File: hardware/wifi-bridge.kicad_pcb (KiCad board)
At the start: 2 copper layers, 63 parts, among them J101 USB-MINI-B-SMD, P201 CON-SENSOR, Q201 MOS_P, SW201 ERASE, SW202 RESET, U101 AT91SAM3SXB, U102 82400152, U103 AAT3681A, U104 PAM2301, U105 FAN4860, U201 ESP8266_WROOM02, U202 M24C64, X201 16MHz

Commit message: new placement idea
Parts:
- removed BT101: BATTERY, kicad-libraries:JST-PH-SM4-2
- removed C110, C111, C112, C115, C116: 100nF, kicad-libraries:0603E
- removed C113, C117: 10µF, kicad-libraries:0805E
- removed C114, C120, C121: 4.7µF, kicad-libraries:0603E
- removed C118, C119: 2.2µF, kicad-libraries:0603E
- removed D201: LED, kicad-libraries:D0603
- removed F101: PTC, kicad-libraries:1206E
- removed FILTER201: Filter-8x, kicad-libraries:DFN16-33x135
- removed J101: USB-MINI-B-SMD, kicad-libraries:USB-MINI-B-SMD
- removed L103: FB, kicad-libraries:0603E
- removed L104: LBR2012T100K, kicad-libraries:0805E
- removed L105: 1µH, kicad-libraries:0805E
- removed L106: 4.7µH, kicad-libraries:0805E
- removed P201: CON-SENSOR, kicad-libraries:CON-SENSOR
- removed Q201: MOS_P, kicad-libraries:SOT23GDS
- removed R104: 3.24k, kicad-libraries:0603E
- removed R105: 470k, kicad-libraries:0603E
- removed R106: 1M, kicad-libraries:0603E
- removed RP201: 4k7, kicad-libraries:0603X4
- removed SW201: ERASE, kicad-libraries:SW_06_SMD
- removed SW202: RESET, kicad-libraries:SW_06_SMD
- removed X201: 16MHz, kicad-libraries:CRYSTAL_3225
- added BT201: BATTERY, kicad-libraries:JST-PH-SM4-2, F.Cu at (24.6, 11.8)
- added C210: 100nF, kicad-libraries:0603E, F.Cu at (-7.47, 11.4)
- added C211: 100nF, kicad-libraries:0603E, F.Cu at (11.6, -2.10)
- added C212: 100nF, kicad-libraries:0603E, F.Cu at (8.95, -0.25)
- added C213: 10µF, kicad-libraries:0805E, F.Cu at (-16.5, -12.2)
- added C214: 4.7µF, kicad-libraries:0603E, F.Cu at (-21.9, -5.95)
- added C215: 100nF, kicad-libraries:0603E, F.Cu at (-23.2, -8.47)
- added C216: 100nF, kicad-libraries:0603E, F.Cu at (-24.8, -1.32)
- added C217: 10µF, kicad-libraries:0805E, F.Cu at (-30.4, -5.58)
- added C218: 2.2µF, kicad-libraries:0603E, F.Cu at (-29.1, -1.15)
- added C219: 2.2µF, kicad-libraries:0603E, F.Cu at (-31.4, -11.2)
- added C220: 4.7µF, kicad-libraries:0603E, F.Cu at (-10.0, -7.12)
- added C221: 4.7µF, kicad-libraries:0603E, F.Cu at (-5.83, -12.1)
- added D101: LED, kicad-libraries:D0603, F.Cu at (-7.47, -9.53)
- added F201: PTC, kicad-libraries:1206E, F.Cu at (163.2, 19.4)
- added FILTER101: Filter-8x, kicad-libraries:DFN16-33x135, F.Cu at (157.5, 47.4)
- added J201: USB-MINI-B-SMD, kicad-libraries:USB-MINI-B-SMD, F.Cu at (155.8, 15.2)
- added L201: FB, kicad-libraries:0603E, F.Cu at (-3.60, -3.70)
- added L202: 744230900, kicad-libraries:WE-CNSW-0603, F.Cu at (153.3, 26.6)
- added L203: FB, kicad-libraries:0603E, F.Cu at (-2.45, -11.4)
- added L204: LBR2012T100K, kicad-libraries:0805E, F.Cu at (-22.4, -13.8)
- added L205: 1µH, kicad-libraries:0805E, F.Cu at (-15.9, -0.23)
- added L206: 4.7µH, kicad-libraries:0805E, F.Cu at (-1.30, -13.3)
- added P101: CON-SENSOR, kicad-libraries:CON-SENSOR, F.Cu at (155.8, 55.2)
- added Q101: MOS_P, kicad-libraries:SOT23GDS, F.Cu at (-25.4, 4.10)
- added R204: 3.24k, kicad-libraries:0603E, F.Cu at (1.93, -8.88)
- added R205: 470k, kicad-libraries:0603E, F.Cu at (2.00, -6.75)
- added R206: 1M, kicad-libraries:0603E, F.Cu at (-1.57, -5.03)
- added RP101: 4k7, kicad-libraries:0603X4, F.Cu at (-9.38, -2.25)
- added SW101: ERASE, kicad-libraries:SW_06_SMD, F.Cu at (4.05, -20.6)
- added SW102: RESET, kicad-libraries:SW_06_SMD, F.Cu at (-13.4, -21.5)
- added U106: DRILL, kicad-libraries:DRILL_NP, F.Cu at (125.3, 17.7)
- added U107: DRILL, kicad-libraries:DRILL_NP, F.Cu at (170.3, 17.7)
- added U203: PAM2301, kicad-libraries:TSOT-25, F.Cu at (-15.1, -4.40)
- added U204: FAN4860, kicad-libraries:UMLP_22, F.Cu at (-17.2, 5.45)
- added X101: 16MHz, kicad-libraries:CRYSTAL_3225, F.Cu at (-2.45, -7.72)
- C101: value 10µF -> 100nF; footprint kicad-libraries:0805E -> kicad-libraries:0603E
- C102: value 100nF -> 470µF; footprint kicad-libraries:0603E -> kicad-libraries:ELKO_63
- C103: value 4.7µF -> 100nF
- C104, C105: value 100nF -> DNP
- C106, C108: value 100nF -> 1µF
- C107: value 2.2µF -> 1µF
- C201: value 100nF -> 10µF; footprint kicad-libraries:0603E -> kicad-libraries:0805E
- C202: value 470µF -> 100nF; footprint kicad-libraries:ELKO_83 -> kicad-libraries:0603E
- C203: value 100nF -> 4.7µF
- C204, C205: value DNP -> 100nF
- C206, C208: value 1µF -> 100nF
- C207: value 1µF -> 2.2µF
- L101: value FB -> INDUCT
- L102: value 744230900 -> INDUCT
- R101, R102: value 27 -> 10k
- R103: value 1R0 -> 2k2
- R201, R202: value 10k -> 27
- R203: value 2k2 -> 1R0
- U102: value 82400152 -> ESP8266_WROOM02; footprint kicad-libraries:SOT563-SPEC -> kicad-libraries:ESP8266_WROOM02
- U103: value AAT3681A -> M24C64; footprint kicad-libraries:SC70JW-8 -> kicad-libraries:SOIC8
- U104: value PAM2301 -> DRILL; footprint kicad-libraries:TSOT-25 -> kicad-libraries:DRILL_NP
- U105: value FAN4860 -> DRILL; footprint kicad-libraries:UMLP_22 -> kicad-libraries:DRILL_NP
- U201: value ESP8266_WROOM02 -> 82400152; footprint kicad-libraries:ESP8266_WROOM02 -> kicad-libraries:SOT563-SPEC
- U202: value M24C64 -> AAT3681A; footprint kicad-libraries:SOIC8 -> kicad-libraries:SC70JW-8
- moved U201 104.6 mm to (156.2, 25.7), turned to 180 degrees
- moved R201 90.6 mm to (150.2, 25.9), turned to 180 degrees
- moved R202 89.8 mm to (150.2, 27.3), turned to 180 degrees
- moved U101 88.4 mm to (155.8, 36.2)
- moved C102 79.4 mm to (127.7, 45.5), turned to 180 degrees
- moved C101 71.6 mm to (131.0, 41.4)
- moved U102 69.4 mm to (133.0, 30.1)
- moved U104 56.7 mm to (170.3, 52.7)
- moved U105 51.1 mm to (125.3, 52.7)
- moved U202 51.0 mm to (118.6, 116.5)
- moved R102 45.1 mm to (140.7, 88.8)
- moved L102 44.9 mm to (141.1, 76.6)
- moved R101 20.1 mm to (115.7, 93.5)
- moved L101 15.9 mm to (139.9, 105.6)
- moved C202 4.72 mm to (181.1, 120.7)
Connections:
- C103 pad 1: 3V3 -> GND
- C103 pad 2: GND -> 3V3
- C104 pad 1: 3V3 -> Net-(C104-Pad1)
- C105 pad 1: 3V3 -> Net-(C105-Pad1)
- C108 pad 1: Net-(C107-Pad1) -> +5V
- C203 pad 1: GND -> 3V3
- C203 pad 2: 3V3 -> GND
- C204 pad 1: Net-(C204-Pad1) -> 3V3
- C205 pad 1: Net-(C205-Pad1) -> 3V3
- C208 pad 1: +5V -> Net-(C207-Pad1)
- L101 pad 1: GND -> Net-(C107-Pad1)
- L101 pad 2: Net-(J101-Pad6) -> 3V3
- L102 pad 1: Net-(L102-Pad1) -> Net-(C109-Pad1)
- L102 pad 2: Net-(L102-Pad2) -> +5V
- L102 pad 3: Net-(L102-Pad3) -> (no net)
- L102 pad 4: Net-(L102-Pad4) -> (no net)
- R101 pad 1: Net-(L102-Pad1) -> (no net)
- R101 pad 2: (no net) -> Net-(R101-Pad2)
- R102 pad 1: Net-(L102-Pad4) -> (no net)
- R102 pad 2: (no net) -> Net-(R102-Pad2)
- R103 pad 1: Net-(C115-Pad1) -> 3V3
- R201 pad 1: (no net) -> Net-(L202-Pad1)
- R201 pad 2: Net-(R201-Pad2) -> D+
- R202 pad 1: (no net) -> Net-(L202-Pad4)
- R202 pad 2: Net-(R202-Pad2) -> D-
- R203 pad 1: 3V3 -> Net-(C215-Pad1)
- U101 pad 1: (no net) -> 3V3
- U101 pad 12: (no net) -> Net-(C207-Pad1)
- U101 pad 17: (no net) -> GND
- U101 pad 18: (no net) -> 3V3
- U101 pad 2: (no net) -> GND
- U101 pad 24: (no net) -> Net-(C207-Pad1)
- U101 pad 39: (no net) -> Net-(SW102-Pad1)
- U101 pad 45: (no net) -> 3V3
- U101 pad 46: (no net) -> GND
- U101 pad 54: (no net) -> Net-(C207-Pad1)
- U101 pad 55: (no net) -> Net-(SW101-Pad1)
- U101 pad 56: (no net) -> D-
- U101 pad 57: (no net) -> D+
- U101 pad 58: (no net) -> 3V3
- U101 pad 60: (no net) -> GND
- U101 pad 61: (no net) -> Net-(C105-Pad1)
- U101 pad 62: (no net) -> Net-(C104-Pad1)
- U101 pad 64: (no net) -> Net-(C215-Pad1)
- U101 pad 7: (no net) -> 3V3
- U101 pad 8: (no net) -> Net-(C207-Pad1)
- U102 pad 1: Net-(J101-Pad2) -> 3V3
- U102 pad 2: GND -> (no net)
- U102 pad 3: Net-(J101-Pad3) -> W-SCL
- U102 pad 4: Net-(L102-Pad2) -> Net-(D101-Pad1)
- U102 pad 5: Net-(F101-Pad1) -> (no net)
- U102 pad 6: Net-(L102-Pad3) -> Net-(R101-Pad2)
- U103 pad 1: Net-(C113-Pad1) -> GND
- U103 pad 2: Net-(R104-Pad1) -> GND
- U103 pad 3: VCC -> GND
- U103 pad 4: Net-(C113-Pad1) -> GND
- U103 pad 5: (no net) -> W-SDA
- U103 pad 6: GND -> W-SCL
- U103 pad 7: GND -> (no net)
- U103 pad 8: GND -> 3V3
- U201 pad 1: 3V3 -> Net-(J201-Pad2)
- U201 pad 2: (no net) -> GND
- U201 pad 3: W-SCL -> Net-(J201-Pad3)
- U201 pad 5: (no net) -> Net-(F201-Pad1)
- U201 pad 6: Net-(R201-Pad2) -> Net-(L202-Pad3)
- U202 pad 1: GND -> Net-(C213-Pad1)
- U202 pad 2: GND -> Net-(R204-Pad1)
- U202 pad 3: GND -> VCC
- U202 pad 4: GND -> Net-(C213-Pad1)
- U202 pad 5: W-SDA -> (no net)
- U202 pad 6: W-SCL -> GND
- U202 pad 7: (no net) -> GND
- U202 pad 8: 3V3 -> GND
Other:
- board outline added: 50 x 40 mm

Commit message: new placement mockup
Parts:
- SW101, SW102: footprint kicad-libraries:SW_06_SMD -> kicad-libraries:TACT-SWITCH
- moved C217 197.7 mm to (164.8, 25.2), turned to 90 degrees
- moved C213 188.9 mm to (168.2, 27.5)
- moved C216 180.3 mm to (150.3, 41.6), turned to 270 degrees
- moved C215 177.3 mm to (147.7, 38.7), turned to 180 degrees
- moved L204 176.9 mm to (146.0, 40.3)
- moved C214 174.9 mm to (146.3, 42.0), turned to 180 degrees
- moved L203 174.6 mm to (167.2, 30.0), turned to 270 degrees
- moved C210 170.3 mm to (160.0, 42.5)
- moved R204 169.4 mm to (168.3, 23.2)
- moved C211 157.1 mm to (164.4, 34.3)
- moved SW102 157.0 mm to (138.8, 16.7)
- moved X101 153.5 mm to (144.5, 36.6), turned to 90 degrees
- moved L201 146.9 mm to (141.4, 19.6)
- moved C212 141.5 mm to (146.9, 31.1), turned to 180 degrees
- moved BT201 137.2 mm to (161.7, 15.6)
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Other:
- outline, holes or cut-outs redrawn

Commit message: placement complete
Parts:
- L102: footprint kicad-libraries:WE-CNSW-0603 -> kicad-libraries:0603E
- moved C219 205.4 mm to (167.7, 39.7), turned to 180 degrees
- moved C218 203.4 mm to (171.2, 34.3), turned to 90 degrees
- moved L205 189.2 mm to (169.6, 36.9), turned to 180 degrees
- moved U204 188.7 mm to (169.2, 34.2)
- moved U203 188.7 mm to (167.6, 42.5)
- moved Q101 187.9 mm to (157.3, 48.0), turned to 180 degrees
- moved C221 186.0 mm to (171.9, 42.6), turned to 270 degrees
- moved C220 183.4 mm to (169.2, 31.9)
- moved L206 180.4 mm to (170.2, 42.6), turned to 90 degrees
- moved R206 169.8 mm to (164.7, 29.2)
- moved R205 166.3 mm to (164.7, 27.8), turned to 180 degrees
- moved RP101 154.5 mm to (138.2, 43.6), turned to 180 degrees
- moved D101 141.4 mm to (124.4, 41.6), turned to 180 degrees
- moved C105 83.5 mm to (144.7, 33.2)
- moved C109 77.8 mm to (144.9, 43.1)
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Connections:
- R103 pad 2: Net-(D101-Pad2) -> Net-(D101-Pad1)
- RP101 pad 5: W-SCL -> W-SDA
- RP101 pad 8: W-SDA -> W-SCL
- U102 pad 4: Net-(D101-Pad1) -> Net-(D101-Pad2)
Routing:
- net W-SCL: track 0.00 -> 5.64 mm
- net Net-(FILTER101-Pad1): track 0.00 -> 3.64 mm
- net Net-(FILTER101-Pad2): track 0.00 -> 3.07 mm
- net Net-(FILTER101-Pad7): track 0.00 -> 3.01 mm
- net Net-(R102-Pad2): track 0.00 -> 2.68 mm
- net Net-(FILTER101-Pad6): track 0.00 -> 2.62 mm
- net W-SDA: track 0.00 -> 2.30 mm
- net Net-(FILTER101-Pad3): track 0.00 -> 2.29 mm
- net Net-(FILTER101-Pad5): track 0.00 -> 2.07 mm
- net Net-(FILTER101-Pad4): track 0.00 -> 2.07 mm
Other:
- board size 50 x 40 mm -> 50 x 35 mm
- net class Default: clearance 0.2 -> 0.15; trace_width 0.25 -> 0.15; via_dia 0.6 -> 0.5; via_drill 0.4 -> 0.15
- net class Power added: clearance 0.15, trace_width 0.3, via_dia 0.7, via_drill 0.4
- rule trace_clearance: 0.2 -> 0.15
- rule trace_min: 0.2 -> 0.15
- rule via_min_drill: 0.3 -> 0.15
- rule via_min_size: 0.4 -> 0.5

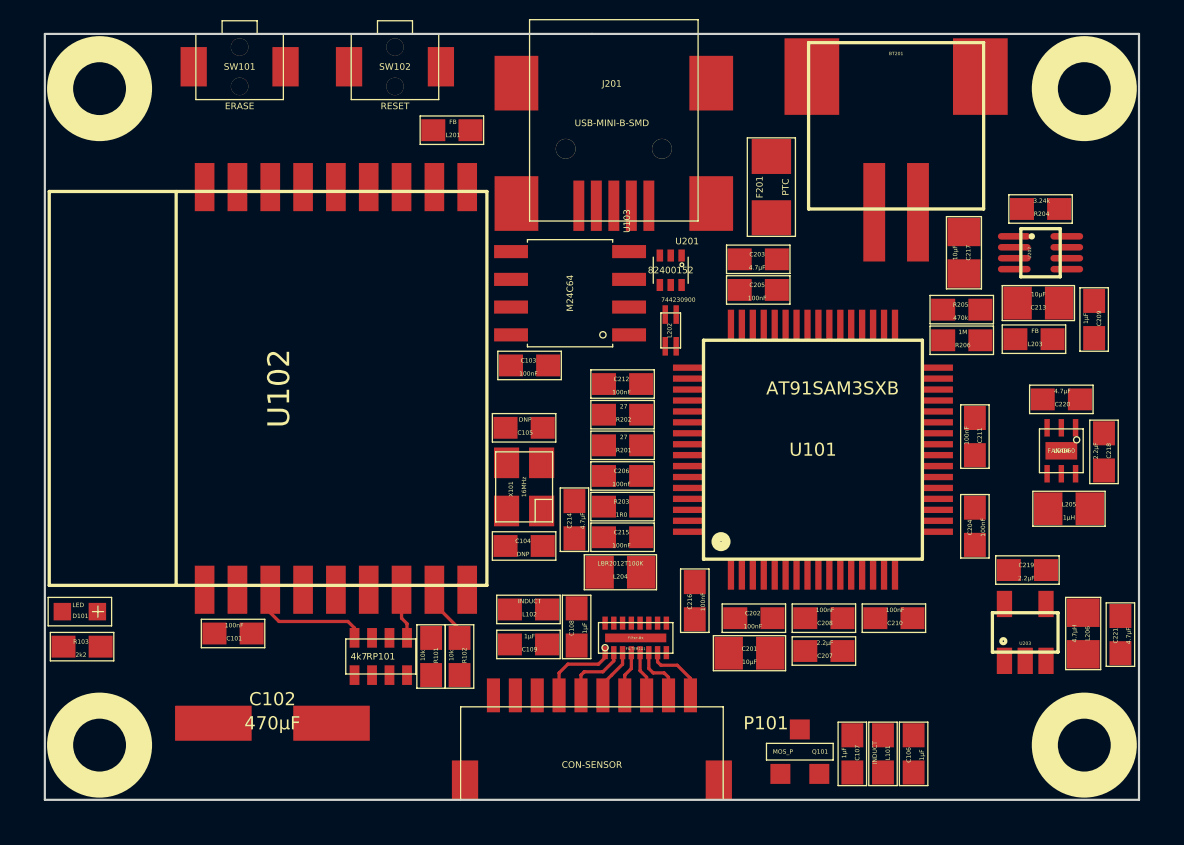
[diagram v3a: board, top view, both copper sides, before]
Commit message: fixed schematic, add tvs diodes, placement changed, clear for routing
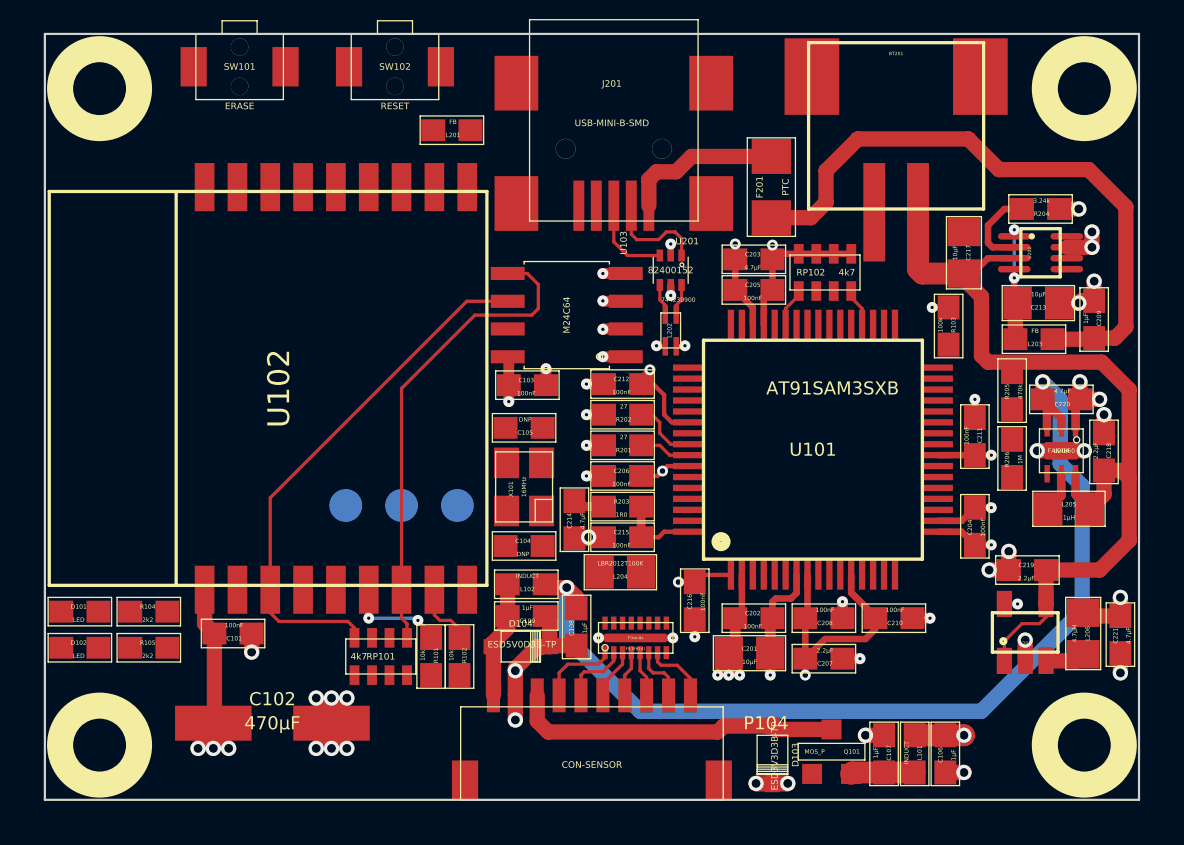
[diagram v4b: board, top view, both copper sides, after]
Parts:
- added D102: LED, kicad-libraries:0603E, F.Cu at (124.4, 43.2)
- added D103: ESD3V3D3B-TP, kicad-libraries:SOD-323, F.Cu at (156.1, 48.1)
- added D104: ESD5V0D3B-TP, kicad-libraries:SOD-323, F.Cu at (144.6, 43.2)
- added P102: CONN_1, kicad-libraries:TSTPT, B.Cu at (139.1, 36.8)
- added P103: CONN_1, kicad-libraries:TSTPT, B.Cu at (141.7, 36.8)
- added P104: CON-SENSOR, kicad-libraries:CON-SENSOR, F.Cu at (147.8, 50.2)
- added R104: 2k2, kicad-libraries:0603E, F.Cu at (127.5, 41.6)
- added R105: 2k2, kicad-libraries:0603E, F.Cu at (127.5, 43.2)
- added RP102: 4k7, kicad-libraries:0603X4, F.Cu at (158.4, 26.1)
- D101: footprint kicad-libraries:D0603 -> kicad-libraries:0603E
- P101: value CON-SENSOR -> CONN_1; footprint kicad-libraries:CON-SENSOR -> kicad-libraries:TSTPT; moved to B.Cu
- R103: value 2k2 -> 100k
- moved R103 42.2 mm to (164.1, 28.6), turned to 90 degrees
- moved P101 17.5 mm to (136.6, 36.8)
- moved R206 5.87 mm to (167.0, 34.6), turned to 270 degrees
- moved R205 4.36 mm to (167.0, 31.5), turned to 270 degrees
- moved C107 1.45 mm to (161.2, 48.1)
- moved L101 1.45 mm to (162.6, 48.1)
- moved C106 1.45 mm to (163.9, 48.1)
- moved Q101 1.45 mm to (158.8, 48.0)
- moved C109 1.30 mm to (144.8, 41.8)
- moved L102 1.15 mm to (144.8, 40.4)
- moved U103 1.01 mm to (146.7, 28.1)
- moved C103 0.91 mm to (144.8, 31.2)
- moved C207 0.35 mm to (158.4, 43.8)
- moved C203 0.20 mm to (155.2, 25.5)
- moved C205 0.20 mm to (155.2, 26.9)
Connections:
- FILTER101 pad 10: (no net) -> B-IO4
- FILTER101 pad 11: (no net) -> B-IO3
- FILTER101 pad 12: (no net) -> B-IO2
- FILTER101 pad 13: (no net) -> B-IO1
- FILTER101 pad 14: (no net) -> B-ADR
- FILTER101 pad 15: (no net) -> B-SDA
- FILTER101 pad 16: (no net) -> B-SCL
- P101 pad 1: Net-(C109-Pad1) -> 3V3
- Q101 pad D: Net-(P101-Pad3) -> Net-(D103-Pad1)
- Q101 pad G: (no net) -> SW-3V3
- R101 pad 1: (no net) -> W-IO15
- R102 pad 1: (no net) -> W-IO0
- R103 pad 1: 3V3 -> CHST
- R103 pad 2: Net-(D101-Pad1) -> 3V3
- U101 pad 10: (no net) -> SW-3V3
- U101 pad 16: (no net) -> VBAT
- U101 pad 21: (no net) -> 5VEN
- U101 pad 3: (no net) -> B-ADR
- U101 pad 30: (no net) -> W-IO0
- U101 pad 31: (no net) -> CHST
- U101 pad 34: (no net) -> W-RXD
- U101 pad 35: (no net) -> W-TXD
- U101 pad 36: (no net) -> B-SCL
- U101 pad 4: (no net) -> B-IO3
- U101 pad 43: (no net) -> B-SDA
- U101 pad 44: (no net) -> W-IO15
- U101 pad 47: (no net) -> W-RST
- U101 pad 48: (no net) -> W-EN
- U101 pad 49: (no net) -> W-GP
- U101 pad 5: (no net) -> B-IO1
- U101 pad 59: (no net) -> LED
- U101 pad 6: (no net) -> B-IO4
- U101 pad 63: (no net) -> B-IO2
- U102 pad 10: (no net) -> W-GP
- U102 pad 11: (no net) -> W-RXD
- U102 pad 12: (no net) -> W-TXD
- U102 pad 15: (no net) -> W-RST
- U102 pad 2: (no net) -> W-EN
- U103 pad 1: GND -> 3V3
- U202 pad 5: (no net) -> CHST
- U204 pad 4: (no net) -> 5VEN
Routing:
- net 3V3: track 0.00 -> 63.3 mm, vias 0 -> 14
- net GND: track 0.00 -> 61.7 mm, vias 0 -> 47
- net +5V: track 0.00 -> 46.4 mm, vias 0 -> 2
- net VCC: track 0.00 -> 41.2 mm
- net Net-(C209-Pad1): track 0.00 -> 28.9 mm
- net Net-(C207-Pad1): track 0.00 -> 20.4 mm, vias 0 -> 3
- net W-SDA: track 2.30 -> 22.0 mm
- net W-SCL: track 5.64 -> 24.4 mm
- net Net-(D103-Pad1): track 0.00 -> 15.0 mm
- net Net-(F201-Pad1): track 0.00 -> 7.71 mm, vias 0 -> 1
- net Net-(R101-Pad2): track 0.00 -> 5.94 mm, vias 0 -> 2
- net Net-(C213-Pad1): track 0.00 -> 5.80 mm, vias 0 -> 2
- net Net-(C109-Pad1): track 0.00 -> 5.40 mm
- net Net-(J201-Pad2): track 0.00 -> 4.75 mm
- net Net-(J201-Pad3): track 0.00 -> 4.01 mm
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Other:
- copper layers 2 -> 4

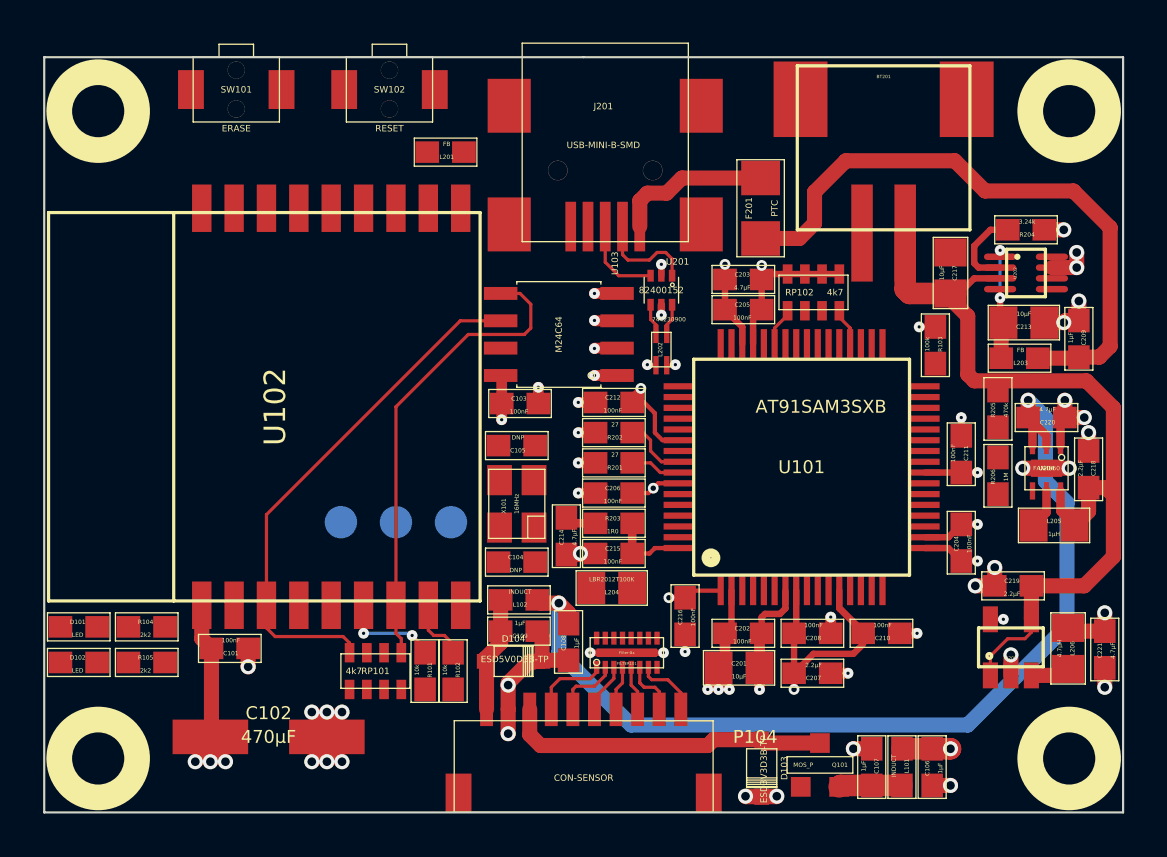
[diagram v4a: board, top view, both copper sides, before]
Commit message: fully routed
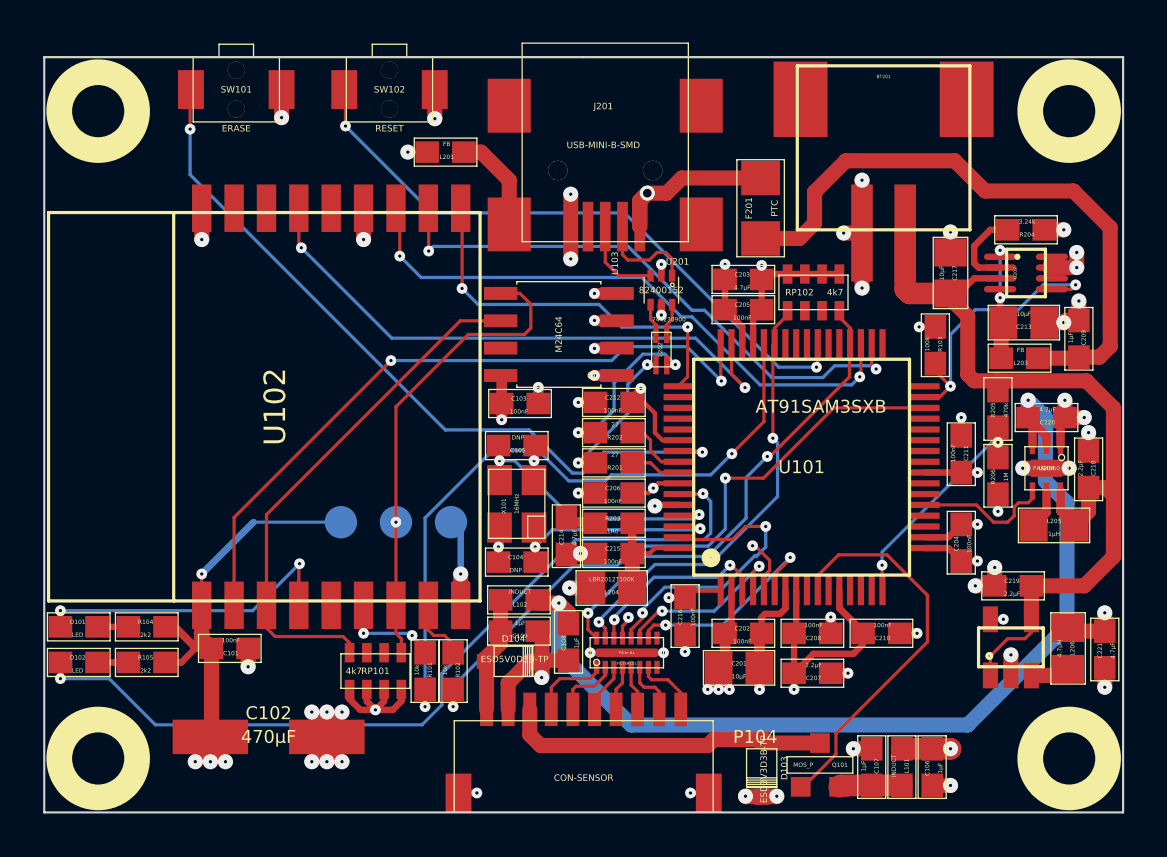
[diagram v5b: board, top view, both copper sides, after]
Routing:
- net GND: track 61.7 -> 280.6 mm, vias 47 -> 64
- net 3V3: track 63.3 -> 210.4 mm, vias 14 -> 16
- net LED: track 0.00 -> 39.4 mm, vias 0 -> 2
- net Net-(C207-Pad1): track 20.4 -> 58.6 mm, vias 3 -> 4
- net Net-(SW101-Pad1): track 0.00 -> 35.0 mm, vias 0 -> 2
- net W-EN: track 0.00 -> 32.3 mm, vias 0 -> 2
- net W-IO15: track 0.00 -> 31.9 mm, vias 0 -> 2
- net W-IO0: track 0.00 -> 30.3 mm, vias 0 -> 2
- net Net-(SW102-Pad1): track 0.00 -> 29.3 mm, vias 0 -> 2
- net W-TXD: track 0.00 -> 27.8 mm, vias 0 -> 2
- net W-RST: track 0.00 -> 27.4 mm, vias 0 -> 2
- net W-RXD: track 0.00 -> 26.9 mm, vias 0 -> 2
- net B-SCL: track 1.73 -> 22.4 mm, vias 0 -> 2
- net B-SDA: track 1.78 -> 20.6 mm, vias 0 -> 2
- net SW-3V3: track 0.00 -> 18.3 mm
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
